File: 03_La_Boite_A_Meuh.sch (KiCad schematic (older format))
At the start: 0 parts

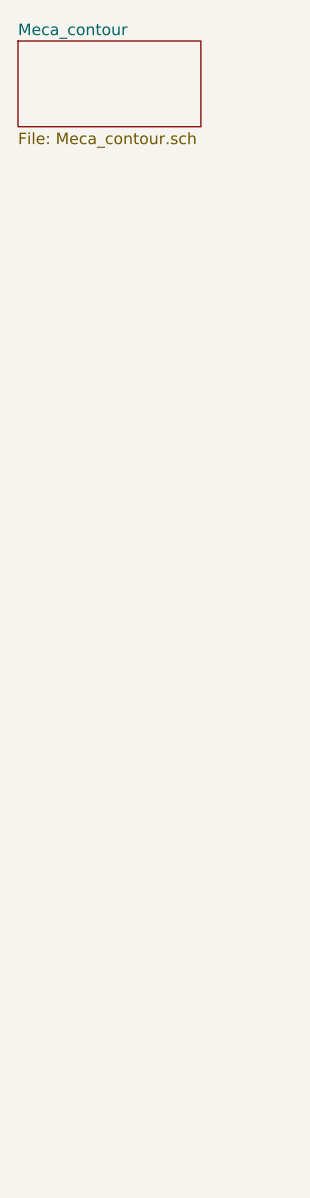
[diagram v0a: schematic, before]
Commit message: add esp32 && mp3 player
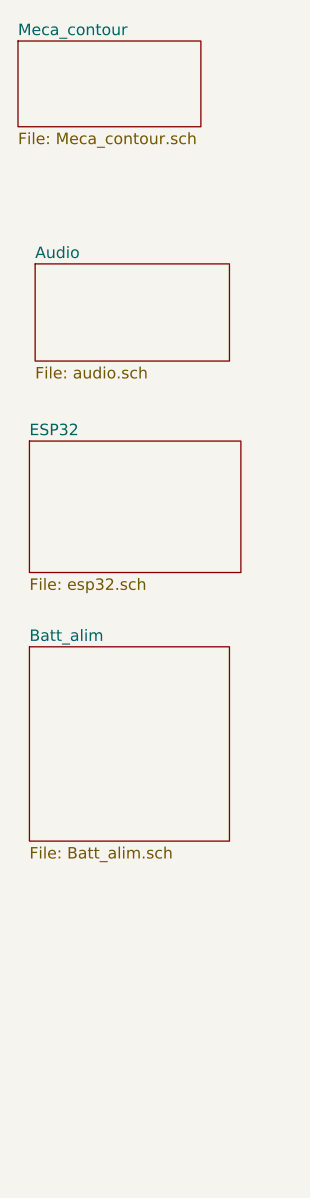
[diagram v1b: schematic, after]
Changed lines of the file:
@@
 $Descr A4 11693 8268
 encoding utf-8
-Sheet 1 2
+Sheet 1 5
 Title ""
 Date ""
@@
 F1 "Meca_contour.sch" 50
 $EndSheet
+$Sheet
+S 1400 2625 850  425
+U 5FC6C772
+F0 "Audio" 50
+F1 "audio.sch" 50
+$EndSheet
+$Sheet
+S 1375 3400 925  575
+U 5FC6D1B4
+F0 "ESP32" 50
+F1 "esp32.sch" 50
+$EndSheet
+$Sheet
+S 1375 4300 875  850
+U 5FC6D1FC
+F0 "Batt_alim" 50
+F1 "Batt_alim.sch" 50
+$EndSheet
 $EndSCHEMATC

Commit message: maj
simplification dfr
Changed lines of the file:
@@
 $Descr A4 11693 8268
 encoding utf-8
-Sheet 1 5
+Sheet 1 6
 Title ""
 Date ""
@@
 F1 "Batt_alim.sch" 50
 $EndSheet
+$Sheet
+S 1525 5700 1000 825
+U 604E9F04
+F0 "tilt" 50
+F1 "tilt.sch" 50
+$EndSheet
 $EndSCHEMATC
